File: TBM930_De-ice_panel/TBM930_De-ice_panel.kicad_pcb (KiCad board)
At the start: 2 copper layers, 190.5 x 101.6 mm, 91 parts, among them J1 SW_AIRFRAME_DE_ICE, J10 AVR-ISP-6, J11 Screw_Terminal_01x02, J2 SW_ICE_LIGHT, J3 SW_PROP_DE_ICE, J4 SW_WIND_SHIELD, J5 SW_PITOT_L_HTR, J6 SW_PITOT_R_HTR, J7 SW_INERT_SEP, J8 Barrel_Jack, J9 USB_B_Mini, SW1 SW_Push, SW2 SW_Push, U1 TLC5917IN, U2 TLC5917IN, U3 ATmega32U4-MU, Y1 Crystal_GND24

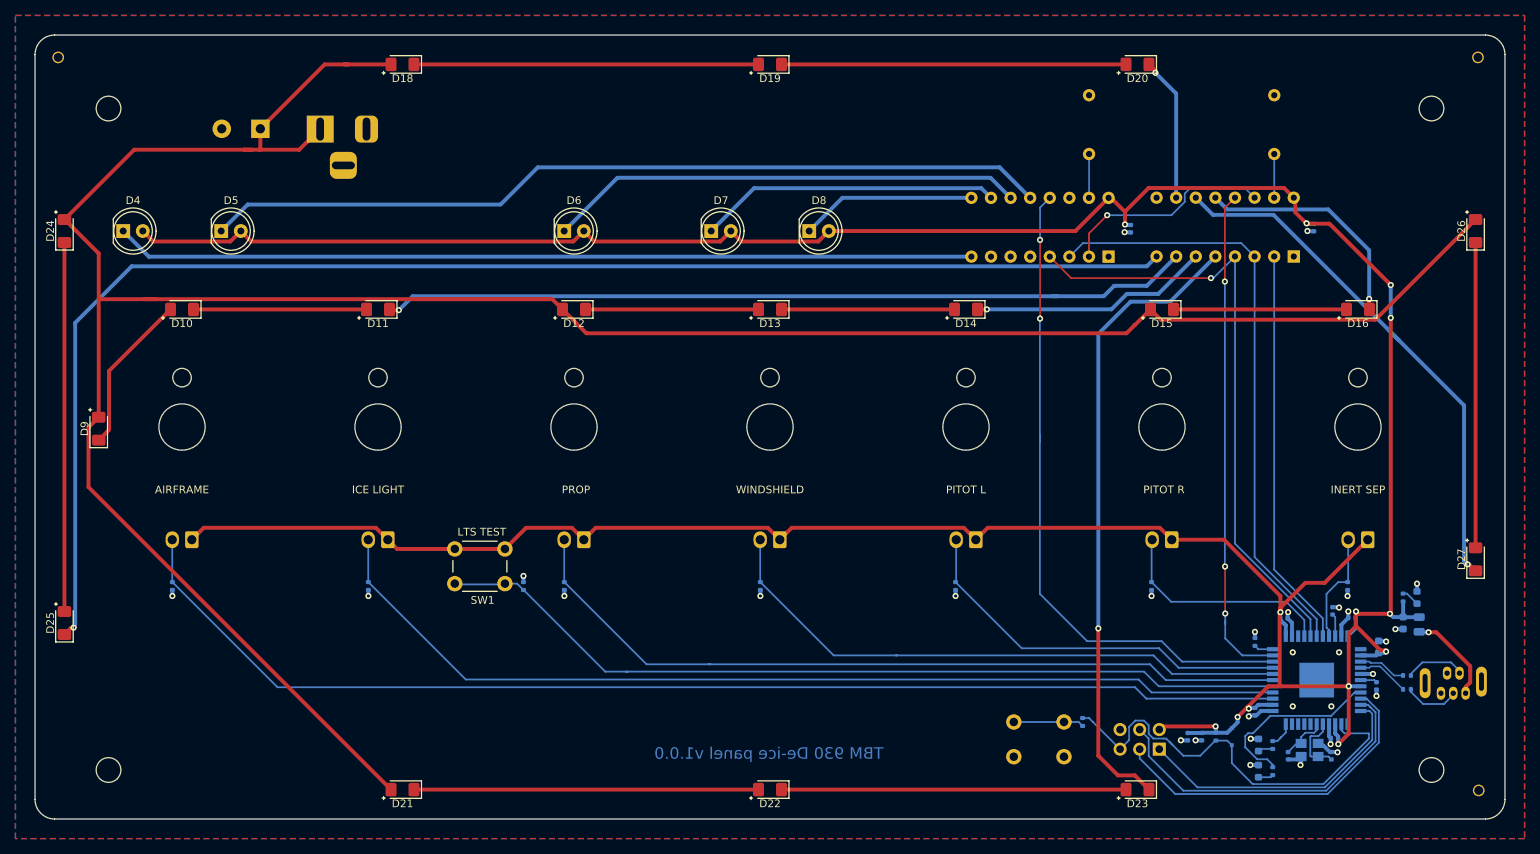
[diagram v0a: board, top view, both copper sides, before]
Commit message: Change footprint for terminal block
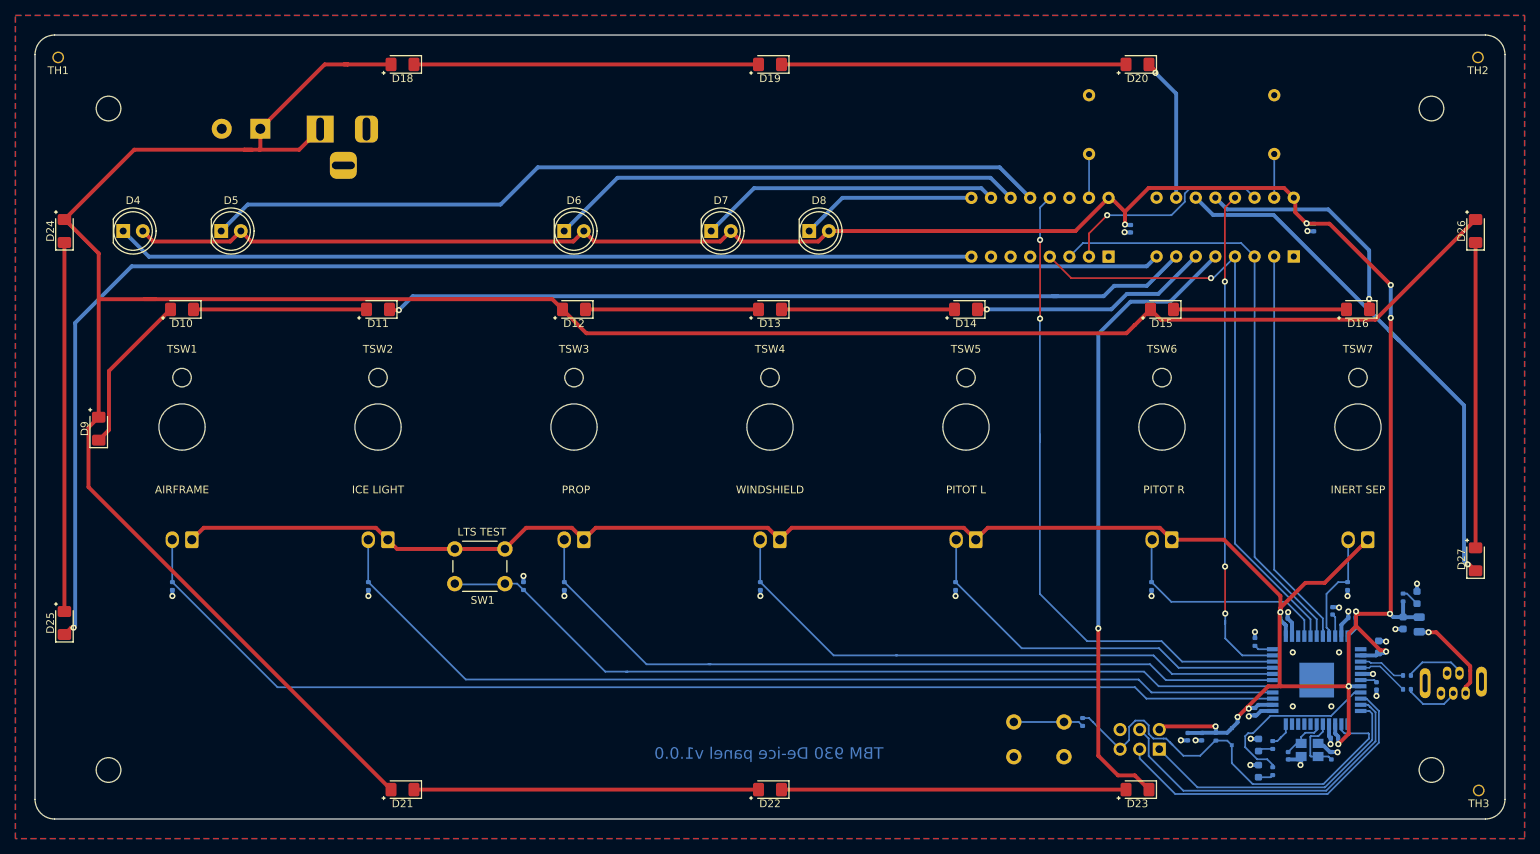
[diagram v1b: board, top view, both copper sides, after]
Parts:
- J11: footprint TerminalBlock_Philmore:TerminalBlock_Philmore_TB132_1x02_P5.00mm_Horizontal -> TerminalBlock_Phoenix:TerminalBlock_Phoenix_PT-1,5-2-5.0-H_1x02_P5.00mm_Horizontal
- TH1, TH2, TH3: footprint Global MobiFlight panel parts:JLCPCB_Tooling_Hole -> TBM930 - De-ice panel:JLCPCB_Tooling_Hole
- TSW1, TSW2, TSW3, TSW4, TSW5, TSW6, TSW7: footprint Global MobiFlight panel parts:MiniToggleSPDT_screw_mount -> TBM930 - De-ice panel:MiniToggleSPDT_screw_mount
